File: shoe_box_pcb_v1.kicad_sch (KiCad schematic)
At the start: 19 parts, among them J1 Barrel_Jack, J2 Conn_01x06_Pin_Male, J3 RFID READER, J4 SOLENOID_CONN, J5 LCD screen, J6 5V BUCK_CONV, Q1 MOSFET, SW2 SW_Push, U2 ATmega328-P, Y1 Crystal 16MHz

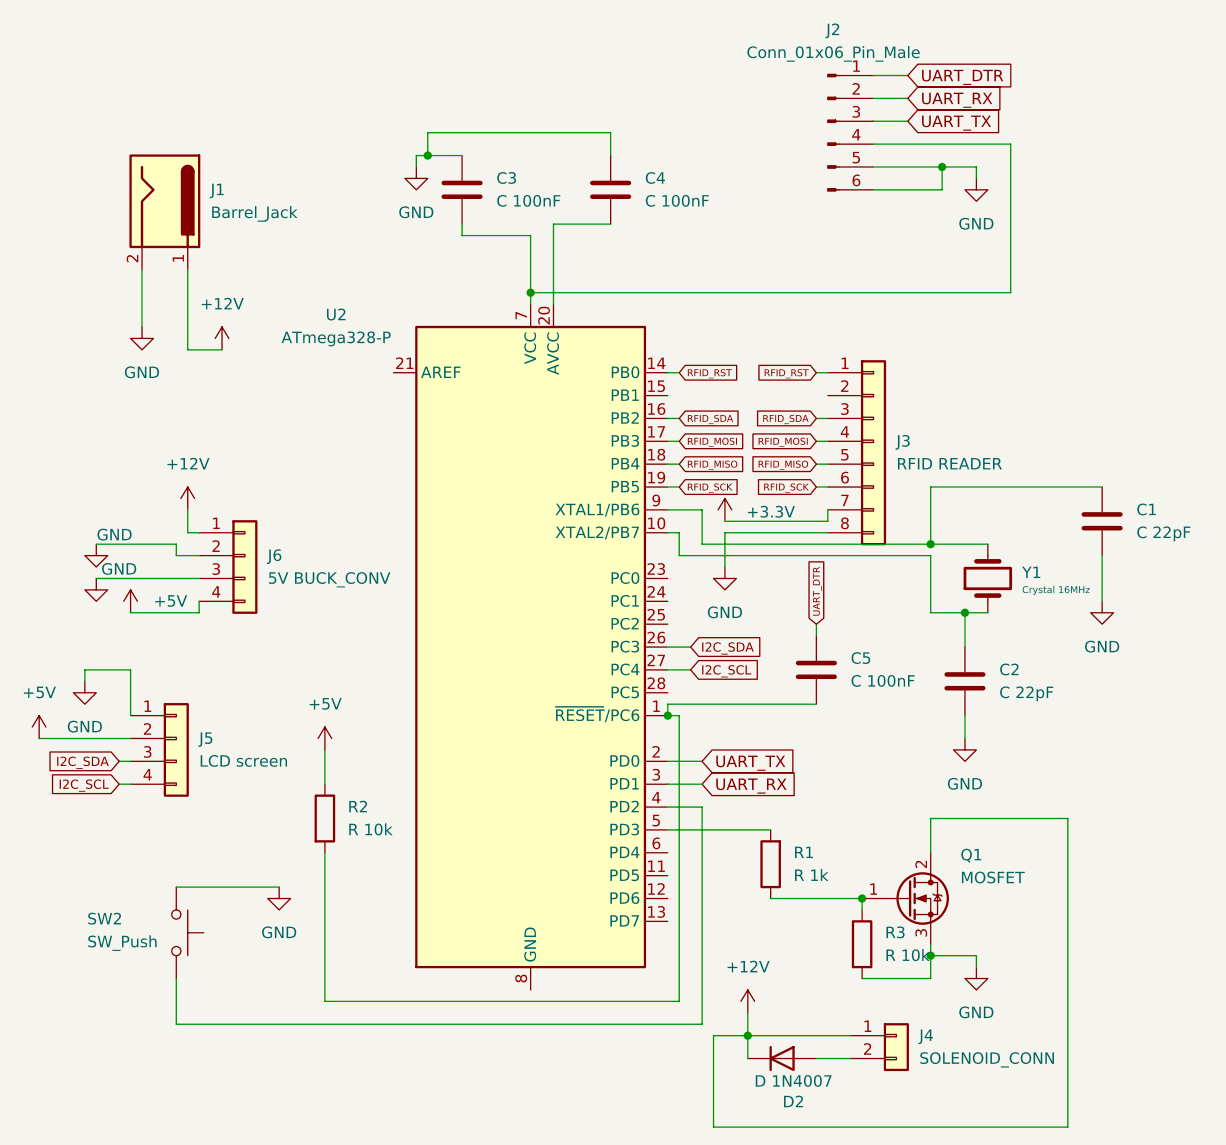
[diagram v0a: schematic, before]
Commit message: updated component names
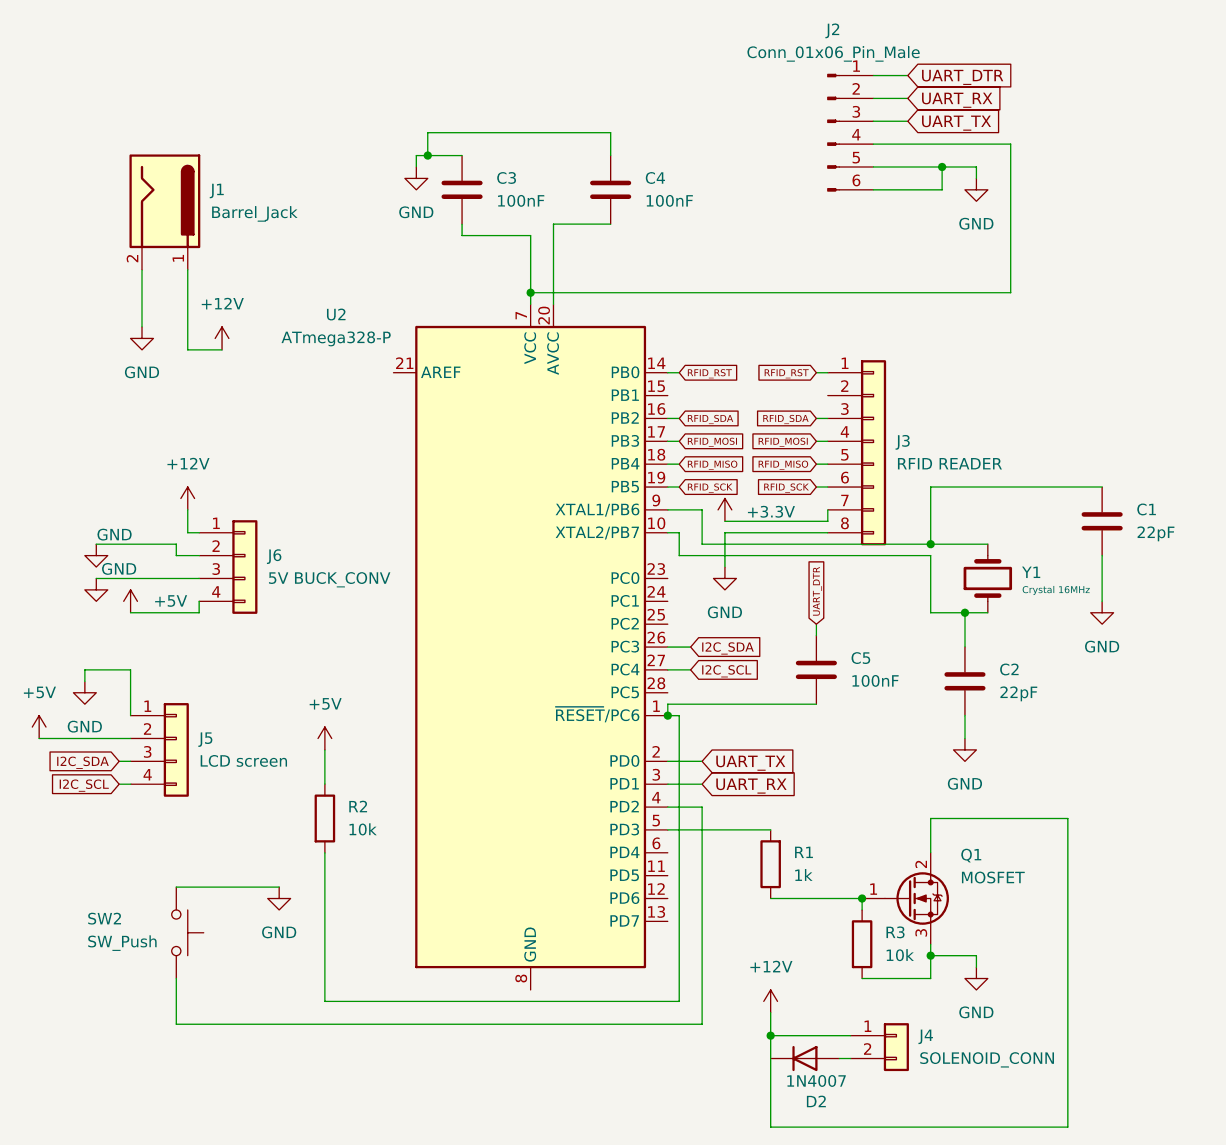
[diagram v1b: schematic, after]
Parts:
- C1, C2: value C 22pF -> 22pF
- C3, C4, C5: value C 100nF -> 100nF
- D2: value D 1N4007 -> 1N4007
- R1: value R 1k -> 1k
- R2, R3: value R 10k -> 10k
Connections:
- net +12V: no longer D2.1 (K)
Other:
- moved on the sheet: D2
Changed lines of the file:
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@@
 	)
 	(junction
-		(at 173.99 143.51)
+		(at 176.53 143.51)
 		(diameter 0)
 		(color 0 0 0 0)
@@
 	(wire
 		(pts
-			(xy 173.99 143.51) (xy 173.99 146.05)
-		)
-		(stroke
-			(width 0)
-			(type default)
-		)
-	)
-	(wire
-		(pts
 			(xy 142.24 53.34) (xy 142.24 54.61)
 		)
@@
 	(wire
 		(pts
-			(xy 170.18 143.51) (xy 173.99 143.51)
-		)
-		(stroke
-			(width 0)
-			(type default)
-		)
-	)
-	(wire
-		(pts
 			(xy 213.36 82.55) (xy 194.31 82.55)
 		)
@@
 	(wire
 		(pts
-			(xy 170.18 153.67) (xy 170.18 143.51)
+			(xy 176.53 143.51) (xy 176.53 153.67)
 		)
 		(stroke
@@
 	(wire
 		(pts
-			(xy 181.61 146.05) (xy 185.42 146.05)
+			(xy 184.15 146.05) (xy 185.42 146.05)
 		)
 		(stroke
@@
 	(wire
 		(pts
-			(xy 170.18 153.67) (xy 209.55 153.67)
+			(xy 176.53 153.67) (xy 209.55 153.67)
 		)
 		(stroke
@@
 	(wire
 		(pts
-			(xy 173.99 140.97) (xy 173.99 143.51)
+			(xy 176.53 140.97) (xy 176.53 143.51)
 		)
 		(stroke
@@
 	(wire
 		(pts
-			(xy 185.42 143.51) (xy 173.99 143.51)
+			(xy 185.42 143.51) (xy 176.53 143.51)
 		)
 		(stroke
@@
 	(symbol
 		(lib_id "power:+12V")
-		(at 173.99 140.97 0)
+		(at 176.53 140.97 0)
 		(unit 1)
 		(body_style 1)
@@
 		(fields_autoplaced yes)
 		(property "Reference" "#PWR09"
-			(at 173.99 144.78 0)
+			(at 176.53 144.78 0)
 			(hide yes)
 			(show_name no)
@@
 		)
 		(property "Value" "+12V"
-			(at 173.99 135.89 0)
+			(at 176.53 135.89 0)
 			(show_name no)
 			(do_not_autoplace no)
@@
 		)
 		(property "Footprint" ""
-			(at 173.99 140.97 0)
+			(at 176.53 140.97 0)
 			(hide yes)
 			(show_name no)
@@
 		)
 		(property "Datasheet" ""
-			(at 173.99 140.97 0)
+			(at 176.53 140.97 0)
 			(hide yes)
 			(show_name no)
@@
 		)
 		(property "Description" "Power symbol creates a global label with name \"+12V\""
-			(at 173.99 140.97 0)
+			(at 176.53 140.97 0)
 			(hide yes)
 			(show_name no)
@@
 			)
 		)
-		(property "Value" "R 1k"
+		(property "Value" "1k"
 			(at 179.07 125.7299 0)
 			(show_name no)
@@
 			)
 		)
-		(property "Value" "C 100nF"
+		(property "Value" "100nF"
 			(at 162.56 50.7999 0)
 			(show_name no)
@@
 			)
 		)
-		(property "Value" "C 22pF"
+		(property "Value" "22pF"
 			(at 217.17 87.6299 0)
 			(show_name no)
@@
 	(symbol
 		(lib_id "Device:D")
-		(at 177.8 146.05 0)
+		(at 180.34 146.05 0)
 		(unit 1)
 		(body_style 1)
@@
 		(dnp no)
 		(property "Reference" "D2"
-			(at 179.07 150.876 0)
+			(at 181.61 150.876 0)
 			(show_name no)
 			(do_not_autoplace no)
@@
 			)
 		)
-		(property "Value" "D 1N4007"
-			(at 179.07 148.59 0)
+		(property "Value" "1N4007"
+			(at 181.61 148.59 0)
 			(show_name no)
 			(do_not_autoplace no)
@@
 		)
 		(property "Footprint" "Package_TO_SOT_THT:TO-220-3_Vertical"
-			(at 177.8 146.05 0)
+			(at 180.34 146.05 0)
 			(hide yes)
 			(show_name no)
@@
 		)
 		(property "Datasheet" ""
-			(at 177.8 146.05 0)
+			(at 180.34 146.05 0)
 			(hide yes)
 			(show_name no)
@@
 		)
 		(property "Description" "Diode"
-			(at 177.8 146.05 0)
+			(at 180.34 146.05 0)
 			(hide yes)
 			(show_name no)
@@
 		)
 		(property "Sim.Device" "D"
-			(at 177.8 146.05 0)
+			(at 180.34 146.05 0)
 			(hide yes)
 			(show_name no)
@@
 		)
 		(property "Sim.Pins" "1=K 2=A"
-			(at 177.8 146.05 0)
+			(at 180.34 146.05 0)
 			(hide yes)
 			(show_name no)
@@
 			)
 		)
-		(property "Value" "R 10k"
+		(property "Value" "10k"
 			(at 129.54 120.6499 0)
 			(show_name no)
@@
 			)
 		)
-		(property "Value" "R 10k"
+		(property "Value" "10k"
 			(at 189.23 134.6199 0)
 			(show_name no)
@@
 			)
 		)
-		(property "Value" "C 100nF"
+		(property "Value" "100nF"
 			(at 146.05 50.7999 0)
 			(show_name no)
@@
 			)
 		)
-		(property "Value" "C 22pF"
+		(property "Value" "22pF"
 			(at 201.93 105.4099 0)
 			(show_name no)
@@
 			)
 		)
-		(property "Value" "C 100nF"
+		(property "Value" "100nF"
 			(at 185.42 104.1399 0)
 			(show_name no)
